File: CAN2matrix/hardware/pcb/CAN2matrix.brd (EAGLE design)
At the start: 41 parts, among them IC1 MEGA8-P, IC2 MCP2515-E/P, IC3 MCP2515-E/P, U1 MCP2551P, U2 MCP2551P, X1 CAN1, X2 CAN2

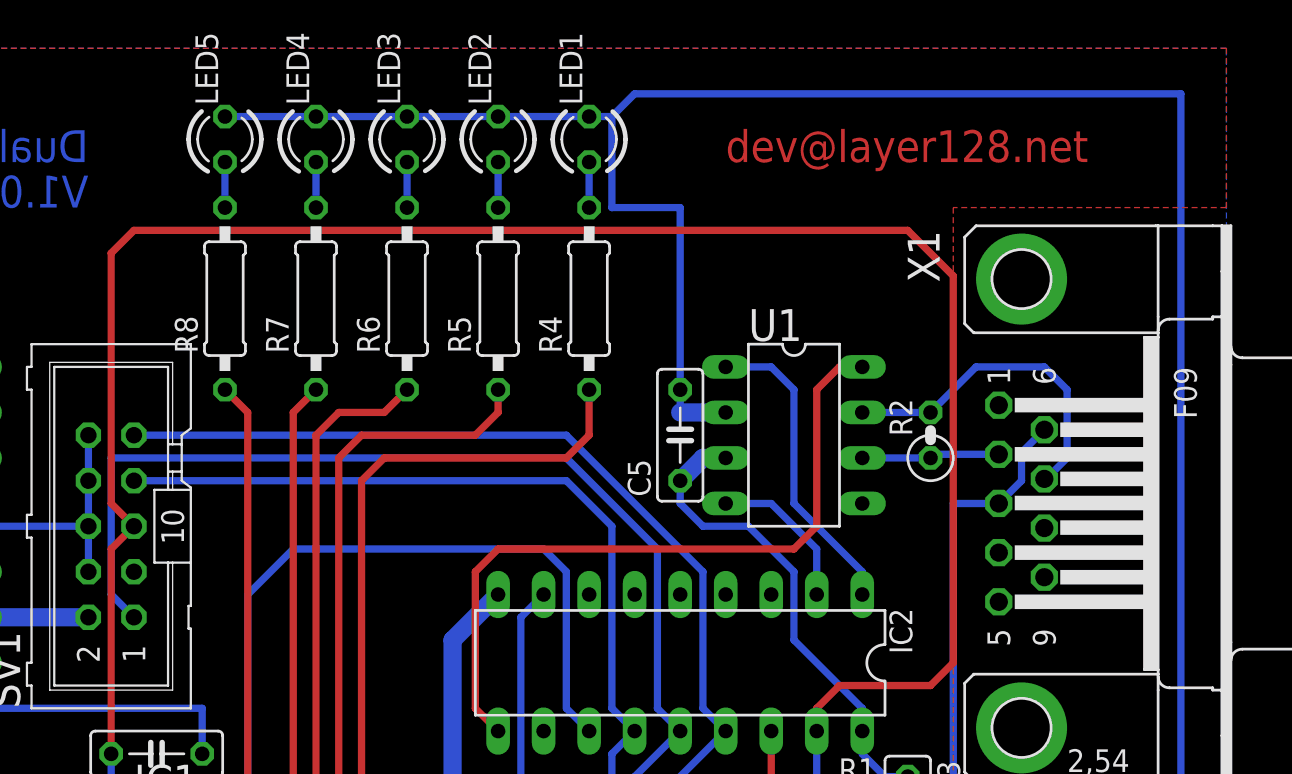
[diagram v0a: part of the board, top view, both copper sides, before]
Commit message: shorten reset wire in top layer
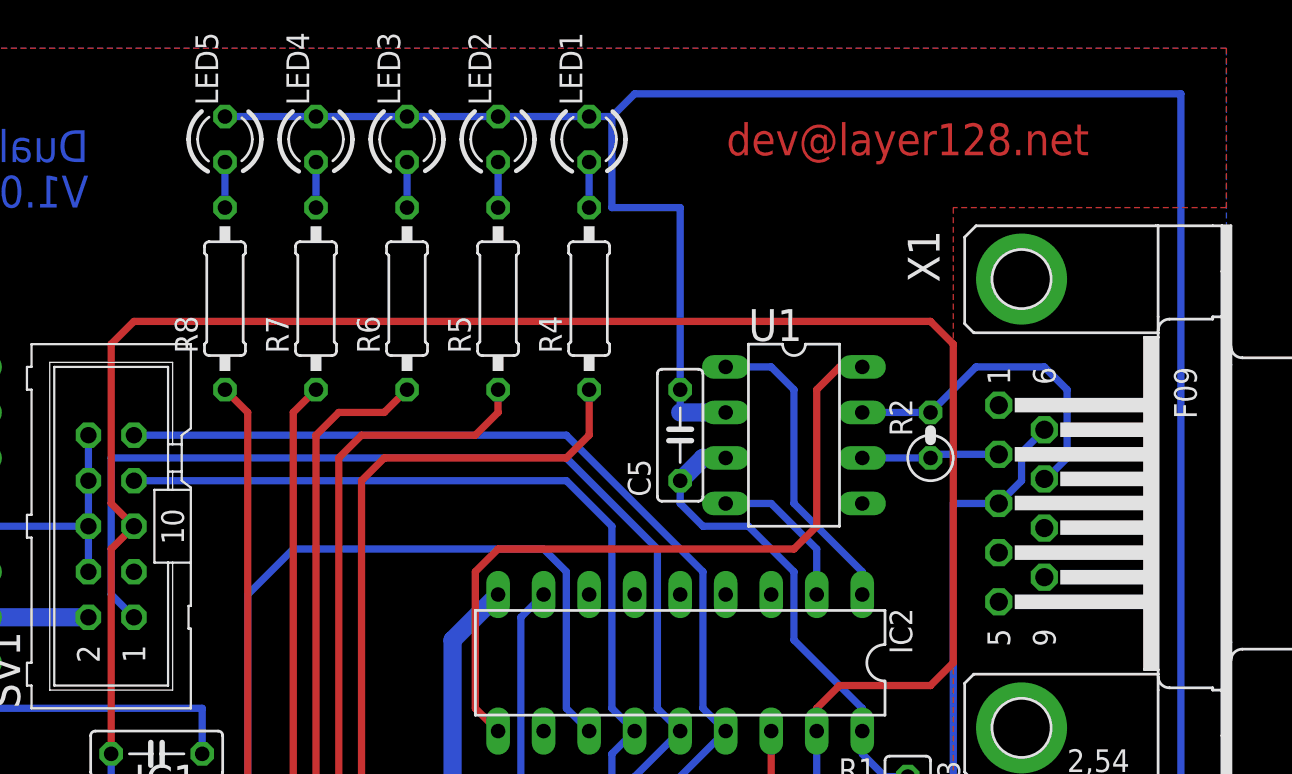
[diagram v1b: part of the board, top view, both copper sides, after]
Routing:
- net N$9: track 148.2 -> 138.8 mm
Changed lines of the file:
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@@
 <layers>
 <layer number="1" name="Top" color="4" fill="1" visible="yes" active="yes"/>
-<layer number="16" name="Bottom" color="1" fill="1" visible="yes" active="yes"/>
+<layer number="16" name="Bottom" color="1" fill="1" visible="no" active="yes"/>
 <layer number="17" name="Pads" color="2" fill="1" visible="yes" active="yes"/>
 <layer number="18" name="Vias" color="2" fill="1" visible="yes" active="yes"/>
@@
 <text x="36.83" y="74.93" size="1.778" layer="16" rot="MR0">Dual CAN</text>
 <text x="36.83" y="72.39" size="1.778" layer="16" rot="MR0">V1.0</text>
-<text x="72.39" y="74.93" size="1.778" layer="1">dev@layer128.net</text>
+<text x="82.55" y="76.2" size="1.778" layer="1" align="center">dev@layer128.net</text>
 <rectangle x1="0" y1="0" x2="100.33" y2="81.28" layer="29"/>
-<rectangle x1="0" y1="0" x2="100.33" y2="81.28" layer="30"/>
 </plain>
 <attributes>
@@
 <wire x1="78.74" y1="45.72" x2="83.82" y2="45.72" width="0.4064" layer="1"/>
 <wire x1="83.82" y1="45.72" x2="85.09" y2="46.99" width="0.4064" layer="1"/>
-<wire x1="85.09" y1="46.99" x2="85.09" y2="68.58" width="0.4064" layer="1"/>
-<wire x1="85.09" y1="68.58" x2="82.55" y2="71.12" width="0.4064" layer="1"/>
-<wire x1="82.55" y1="71.12" x2="39.37" y2="71.12" width="0.4064" layer="1"/>
-<wire x1="39.37" y1="71.12" x2="38.1" y2="69.85" width="0.4064" layer="1"/>
-<wire x1="38.1" y1="69.85" x2="38.1" y2="55.88" width="0.4064" layer="1"/>
+<wire x1="85.09" y1="46.99" x2="85.09" y2="64.77" width="0.4064" layer="1"/>
+<wire x1="85.09" y1="64.77" x2="83.82" y2="66.04" width="0.4064" layer="1"/>
+<wire x1="83.82" y1="66.04" x2="39.37" y2="66.04" width="0.4064" layer="1"/>
+<wire x1="39.37" y1="66.04" x2="38.1" y2="64.77" width="0.4064" layer="1"/>
+<wire x1="38.1" y1="64.77" x2="38.1" y2="55.88" width="0.4064" layer="1"/>
 <wire x1="77.47" y1="10.16" x2="78.74" y2="11.43" width="0.4064" layer="1"/>
 <wire x1="78.74" y1="11.43" x2="78.74" y2="19.05" width="0.4064" layer="1"/>
